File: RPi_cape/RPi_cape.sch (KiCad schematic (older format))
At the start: 93 parts, among them J1 Conn_01x04, J10 Conn_01x02, J11 Conn_01x02, J12 Conn_01x02, J2 Conn_01x02, J3 Conn_01x02, J4 Conn_01x02, J5 Conn_01x03, J6 Conn_01x03, J7 Conn_01x02, J8 Conn_02x20_Odd_Even, J9 Conn_01x02, U1 TL431A, U2 ADC128D818, U3 ADC128D818

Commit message: Extra info, post-design-review fixes
Added extra info on existing alternate circuit options
Added extra info on parts selection
Created initial PCB file
Added bulk cap to +5V input
Design review fixes:
Moved Raspberry Pi PWM output to GPIO18 to take advantage of hardware PWM
Fixed floating shutdown input on audio amp
Added series resistor R177 to allow low battery output to signal to both CPLD and external LED at the same time
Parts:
- added C112: 100uF 50V AlPoly, Capacitor_SMD:CP_Elec_10x10.5, symbol Device:CP1
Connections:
- net +5V: now also C112.1
- net Comms3: now also J8.16 (Pin_16); no longer J8.12 (Pin_12)
- net Comms4: now also J8.18 (Pin_18); no longer J8.16 (Pin_16)
- net Comms5: now also J8.22 (Pin_22); no longer J8.18 (Pin_18)
- net Comms6: now also J8.23 (Pin_23); no longer J8.22 (Pin_22)
- net GND: now also C112.2
- net GPIO13 renamed RPi_PWM2
- net GPIO19 renamed RPi_PWM3
- net GPIO26 renamed RPi_PWM4
- net GPIO6: no longer names the net of J8.31 (Pin_31)
- net GPIO6: no longer R25.2
- net sheet5EEB3F4D/En renamed 5V Regulator (other)/En
- new net RPi_PWM1: J8.12 (Pin_12), R25.2
- no-connect marks 2 -> 8
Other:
- note added: "GPIO11"
- note added: "GPIO13"
- note added: "GPIO19"
- note added: "GPIO26"
- moved on the sheet: C11, C12, C13, C14, C15, C16, C17, C18, J10, J11, J12, J9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

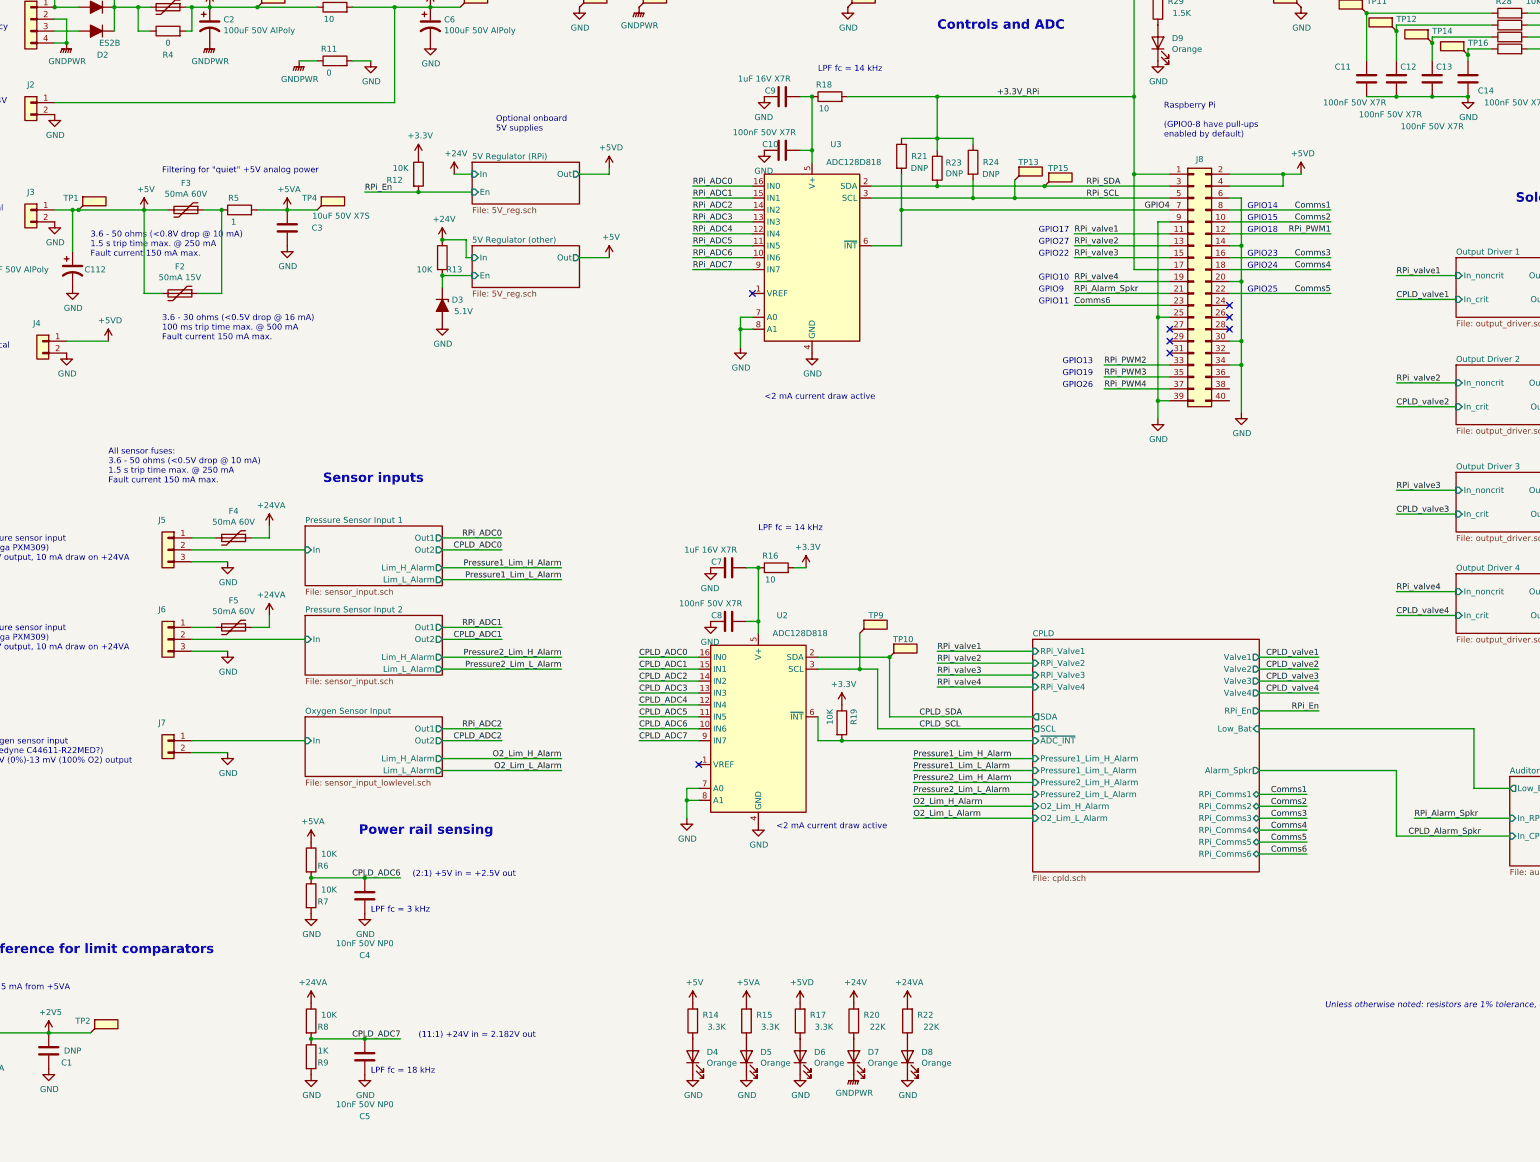
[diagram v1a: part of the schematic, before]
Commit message: Finished schematic, most of PCB placement
Added error budget for analog inputs
Finished most of PCB placement and started routing
Added R185, R186 to allow powering CPLD from alarm power for better power-down alarm sound flexibility
Changed power-down alarm monitoring from +5VD to +3.3V, and put +5VA and +24VA monitoring as DNP by default, to match the CPLD's ability to run off backup battery and monitor +5VA/+24VA
Moved from 3x AA (4.5V) to 4x AA (6V) alarm battery for better audio voltage, and added PNP diode-ORing circuit (Q12 etc.) to accomodate higher voltage, changed low-battery threshold to 5V
Added pull-down resistors to sensor op-amp outputs to help extend low-end output range
Changed 1nF, 10nF, 100nF caps to 0603-size for better fit of CPLD decoupling caps
Added additional bulk cap C19 to audio amp's supply just in case of alarm-induced supply fluctuations
Decreased CPLD's I2C pull-up values to deal with anticipated PCB capacitance etc.
Removed additional dual-op-amp footprint option on analog inputs, due to high availability of single op-amps
Adjusted O2 sensor input clamping to reduce errors from diode leakage current (changed from zener to low-leakage clamps to rails)
Changed O2 sensor op-amp to different lower-offset part to reduce total error from +/- 4.2% FS to +/- 1.7% FS
Fixed missing power section for U17
Added rotary encoder input
Consolidated +5VA fuse options
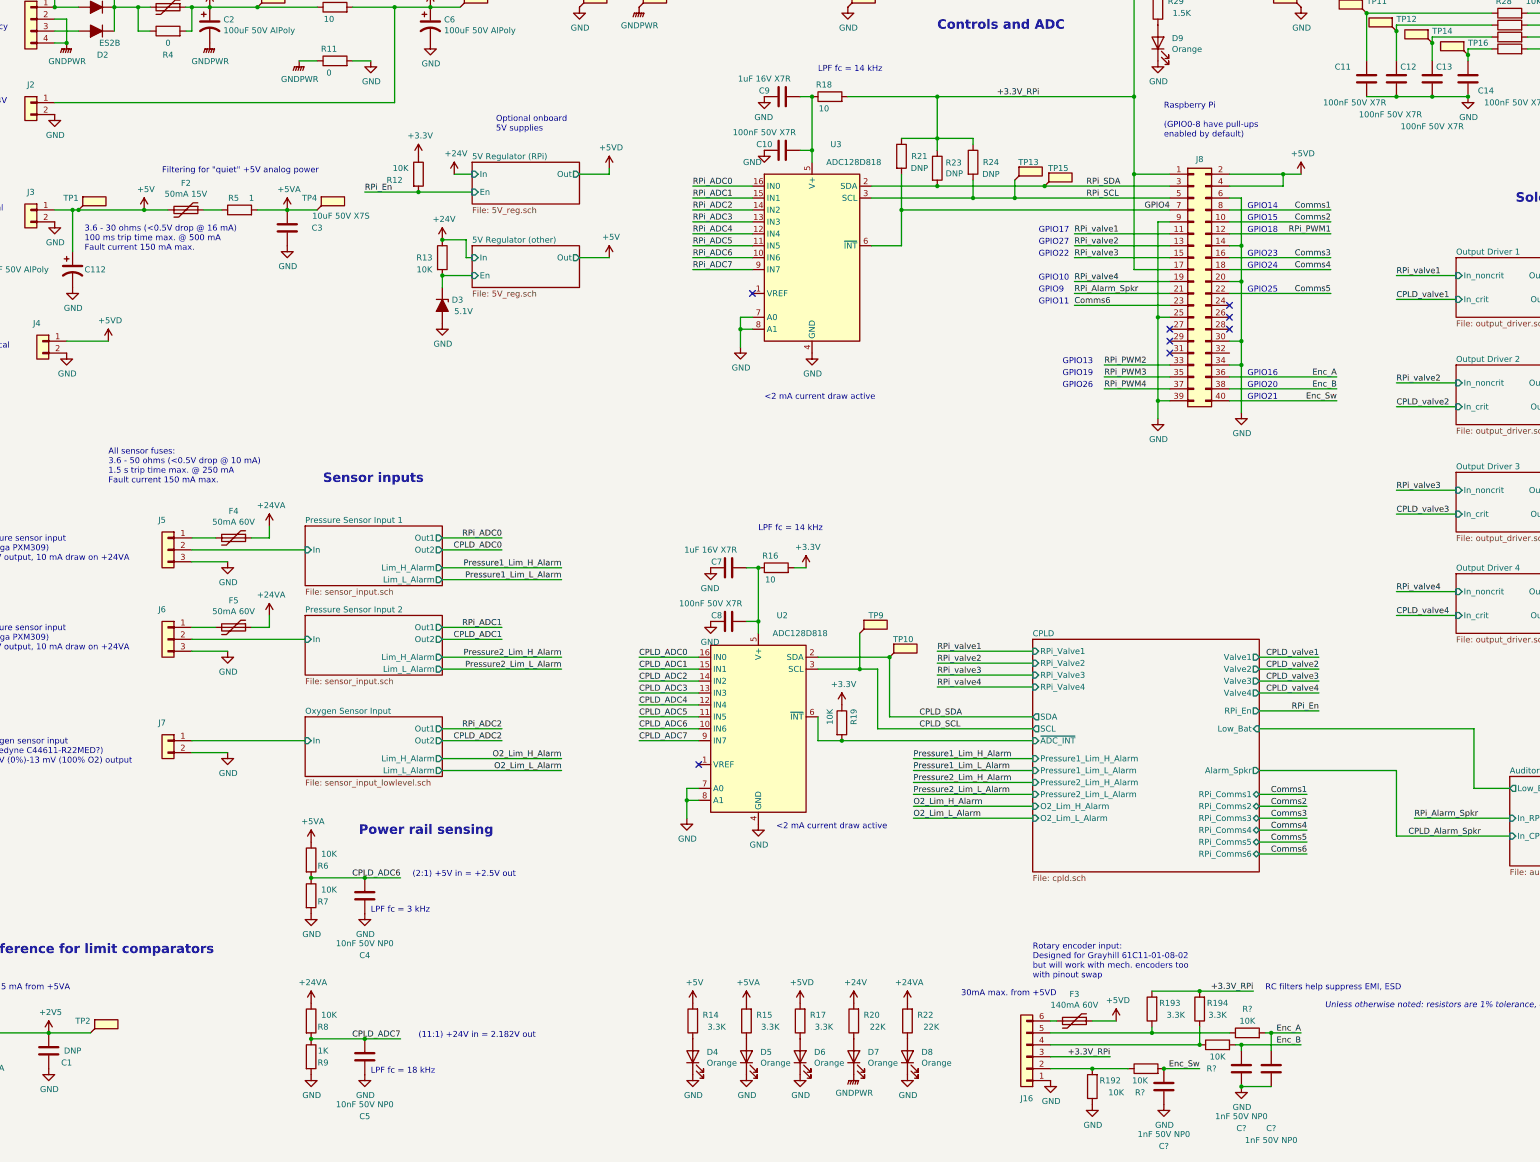
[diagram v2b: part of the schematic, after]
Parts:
- added C? (x3): 1nF 50V NP0, Capacitor_SMD:C_0603_1608Metric, symbol Device:C
- added J16: Conn_01x06, Connector_PinSocket_2.54mm:PinSocket_1x06_P2.54mm_Vertical, symbol Connector_Generic:Conn_01x06
- added R192, R? (x3): 10K, Resistor_SMD:R_1206_3216Metric, symbol Device:R
- added R193, R194: 3.3K, Resistor_SMD:R_1206_3216Metric, symbol Device:R
- C10, C11, C12, C13, C14, C8: footprint Capacitor_SMD:C_0805_2012Metric -> Capacitor_SMD:C_0603_1608Metric; Part Number 08055C104KAT2A -> 06035C104JAT2A
- C4, C5: footprint Capacitor_SMD:C_0805_2012Metric -> Capacitor_SMD:C_0603_1608Metric; Manufacturer Samsung -> Murata; Part Number CL21C103JBFNNNG -> GRM1885C1H103JA01D
- F3: value 50mA 60V -> 140mA 60V; footprint Fuse:Fuse_1206_3216Metric -> Fuse:Fuse_1812_4532Metric; Part Number 0ZCJ0005FF2E -> 0ZCG0014FF2C
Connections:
- net +3.3V_RPi: now also J16.3 (Pin_3), R193.2, R194.2
- net +5V: no longer F3.2
- net +5VD: now also F3.1
- net GND: now also C?.1, C?.1, C?.1, J16.1 (Pin_1), R192.1
- net Enc_A: now reaches J8.36 (Pin_36)
- net Enc_A: now also C?.2, R?.2
- net Enc_B: now reaches J8.38 (Pin_38)
- net Enc_B: now also C?.2, R?.2
- net Enc_Sw: now reaches J8.40 (Pin_40)
- net Enc_Sw: now also C?.2, R?.2
- net at F2.1, R5.1: no longer F3.1
- new net: J16.2 (Pin_2), R192.2, R?.1
- new net: J16.4 (Pin_4), R194.1, R?.1
- new net: J16.5 (Pin_5), R193.1, R?.1
- new net: F3.2, J16.6 (Pin_6)
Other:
- note added: "30mA max. from +5VD"
- note added: "GPIO16"
- note added: "GPIO20"
- note added: "GPIO21"
- note added: "RC filters help suppress EMI, ESD"
- note added: "Rotary encoder input:\nDesigned for Grayhill 61C11-01-08-02\nbut will work with mech. encoders too\nwith pinout swap"
- note removed: "3.6 - 50 ohms (<0.8V drop @ 10 mA)\n1.5 s trip time max. @ 250 mA\nFault current 150 mA max."
- moved on the sheet: F2

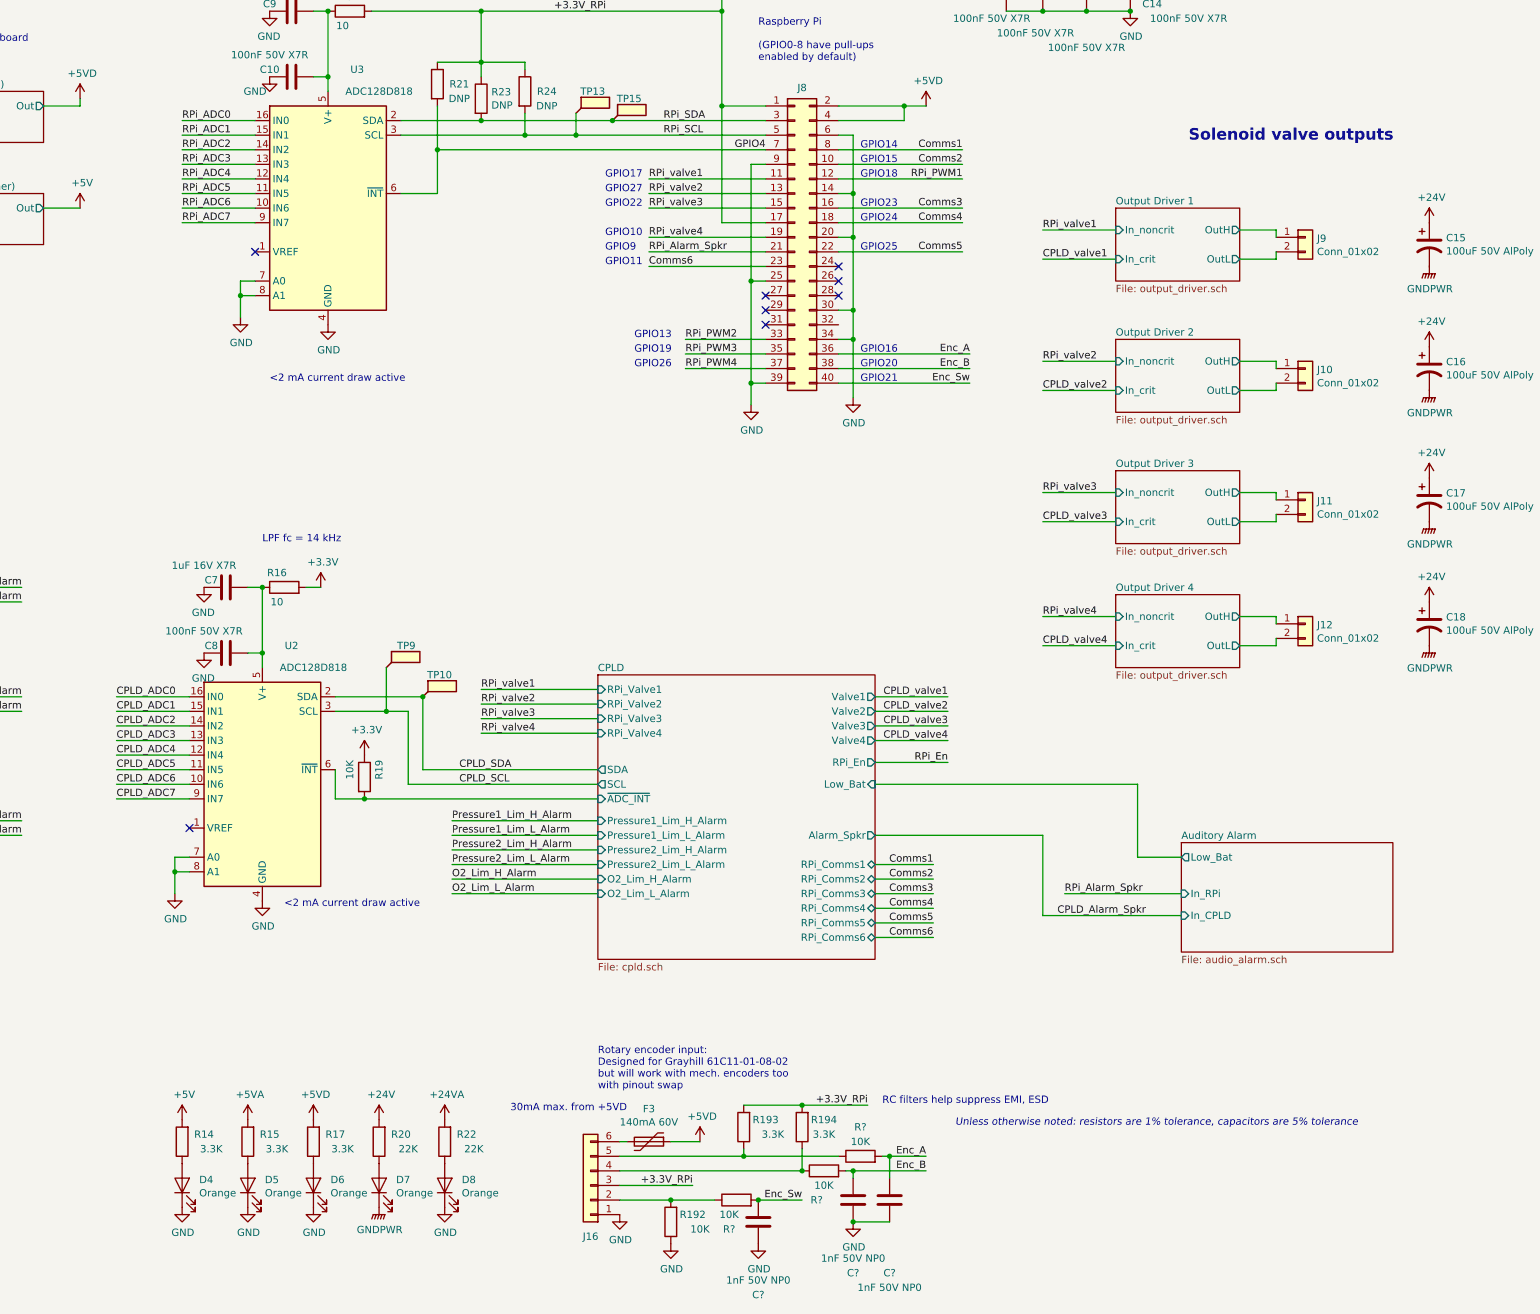
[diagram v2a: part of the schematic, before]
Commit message: Finished layout, minor design changes
Assigned CPLD pins
Finished routing PCB
Moved rotary encoder inputs to CPLD
Removed separate decoupling caps for smaller CPLD footprint due to routing constraints
Added pull-downs on CPLD inputs for each valve driver (R198 etc.)
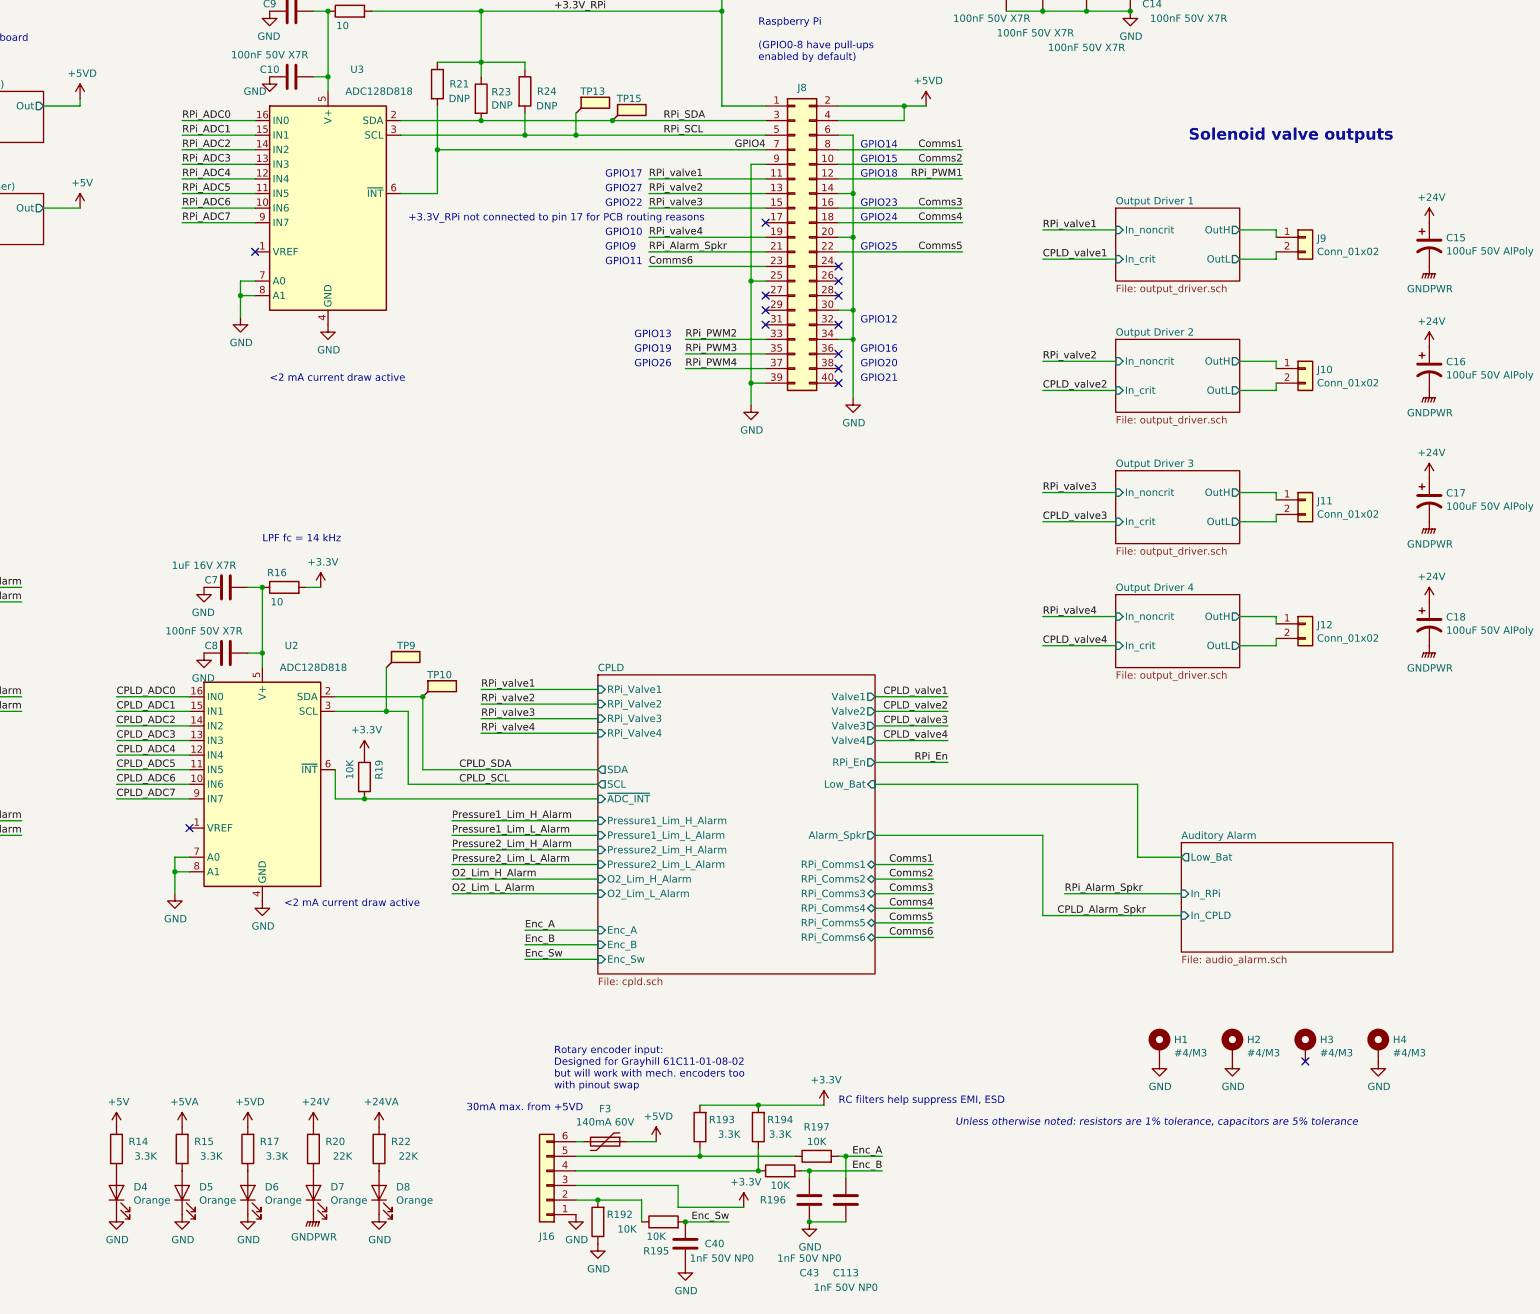
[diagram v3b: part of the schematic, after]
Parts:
- added H1, H2, H3, H4: #4/M3, MountingHole:MountingHole_3.2mm_M3_Pad_Via, symbol Mechanical:MountingHole_Pad
- gave numbers to parts that had none: 6
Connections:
- net +3.3V_RPi: no longer J16.3 (Pin_3), J8.17 (Pin_17), R193.2, R194.2
- net +3V3: now also J16.3 (Pin_3), R193.2, R194.2
- net Enc_A: no longer J8.36 (Pin_36)
- net Enc_B: no longer J8.38 (Pin_38)
- net Enc_Sw: no longer J8.40 (Pin_40)
- net GND: now also H1.1, H2.1, H4.1
- no-connect marks 8 -> 14
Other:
- note added: "+3.3V_RPi not connected to pin 17 for PCB routing reasons"
- note added: "GPIO12"
- moved on the sheet: C113, C40, C43, D4, D5, D6, D7, D8, F3, J16, R14, R15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

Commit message: Digital pressure sensors
Added two digital pressure sensors each, on Raspberry Pi and CPLD I2C busses; preliminary layout only until mechanical details are finalized
Added gnd plane on bottom layer for heatsinking 5V regulators
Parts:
- added H5: #4/M3, MountingHole:MountingHole_3.2mm_M3_Pad_Via, symbol Mechanical:MountingHole_Pad
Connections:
- net GND: now also H5.1
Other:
- note added: "Both sensor fuses:\n3.6 - 50 ohms (<0.5V drop @ 10 mA)\n1.5 s trip time max. @ 250 mA\nFault current 150 mA max."
- note removed: "All sensor fuses:\n3.6 - 50 ohms (<0.5V drop @ 10 mA)\n1.5 s trip time max. @ 250 mA\nFault current 150 mA max."
- moved on the sheet: C4, C5, F4, F5, J5, J6, J7, R6, R7, R8, R9
